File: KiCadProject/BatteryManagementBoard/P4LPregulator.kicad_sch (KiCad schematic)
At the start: 6 parts, among them U401 BD433M5FP

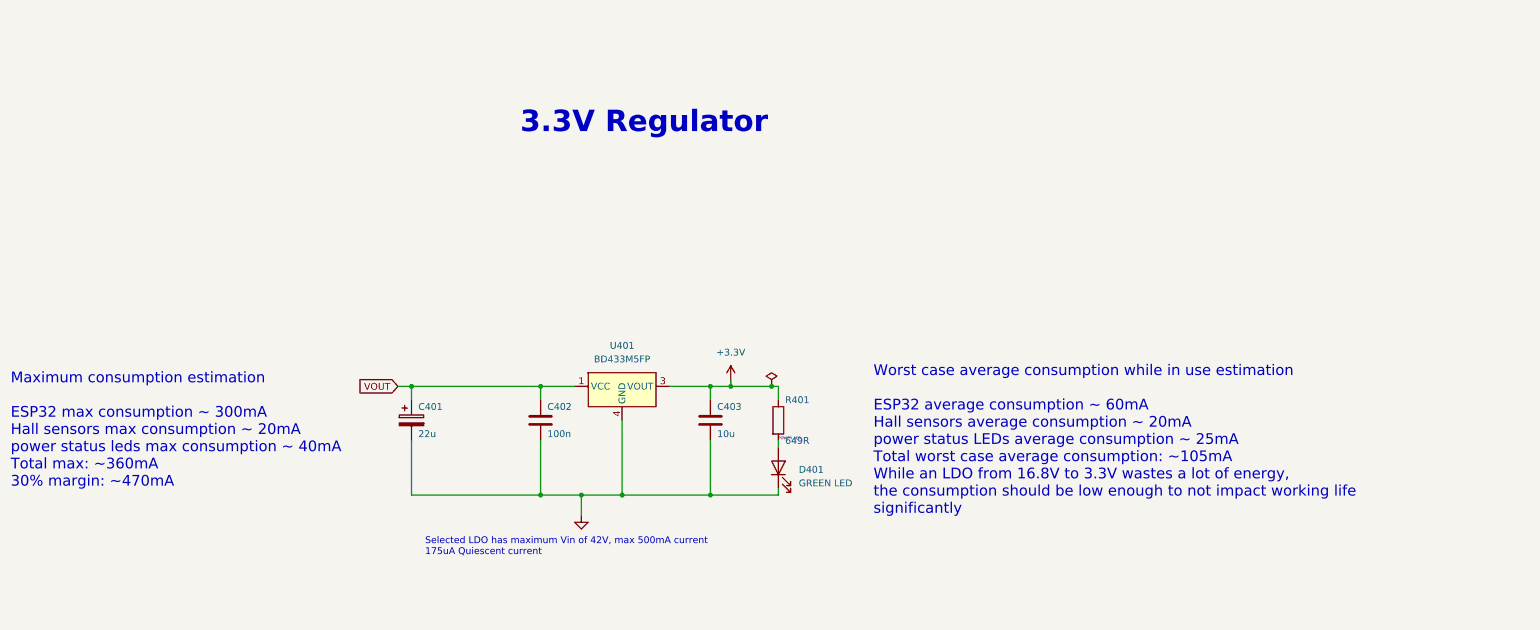
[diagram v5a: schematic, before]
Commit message: All PCB's should be done. Do a final check before ordering.
Signed-off-by: Eldalote.Electronics <Eldalote.Electronics@gmail.com>
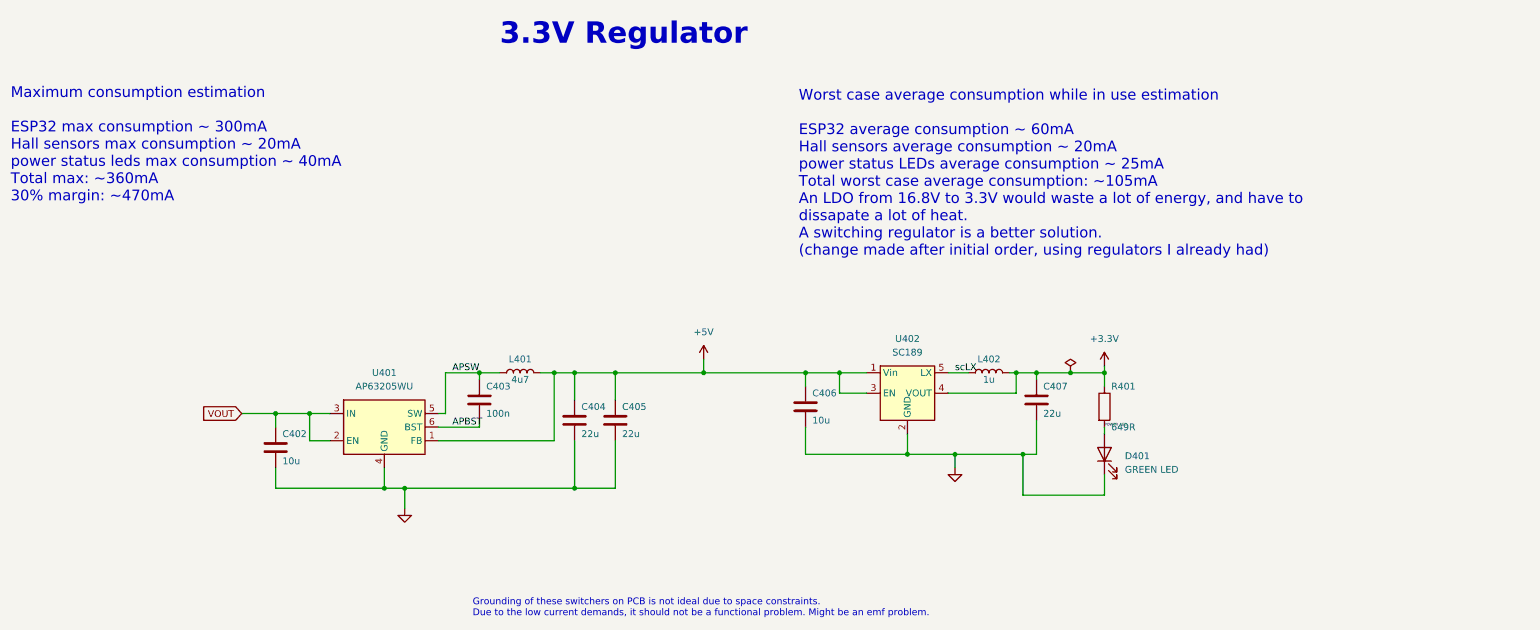
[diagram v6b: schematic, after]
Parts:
- removed C401: 22u, Capacitor_SMD:CP_Elec_5x5.3, symbol Device:C_Polarized
- removed U401: BD433M5FP, Package_TO_SOT_SMD:TO-252-3_TabPin4, symbol Eldalote_symbols:BD433M5FP
- added C404, C405, C407: 22u, Capacitor_SMD:C_0805_2012Metric, symbol Device:C
- added C406: 10u, Capacitor_SMD:C_0805_2012Metric, symbol Device:C
- added L401: 4u7, Inductor_SMD:L_1210_3225Metric, symbol Device:L
- added L402: 1u, Inductor_SMD:L_1210_3225Metric, symbol Device:L
- added U401: AP63205WU, Package_TO_SOT_SMD:TSOT-23-6, symbol Regulator_Switching:AP63205WU
- added U402: SC189, Package_TO_SOT_SMD:SOT-23-5, symbol Eldalote_symbols:SC189
- C402: value 100n -> 10u; footprint Capacitor_SMD:C_0402_1005Metric -> Capacitor_SMD:C_0805_2012Metric; Extra Requirement 25V -> (none); MfID CL05A104KA5NNNC -> (none)
- C403: value 10u -> 100n; footprint Capacitor_SMD:C_0805_2012Metric -> Capacitor_SMD:C_0402_1005Metric; Extra Requirement 25V -> (none); MfID CL21A106KAYNNNG -> (none)
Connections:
- net +3.3V: now also C407.1, L402.2, U402.4 (VOUT); no longer C403.1
- net GND: now also C404.2, C405.2, C406.2, C407.2, U401.4 (GND), U402.2 (GND); no longer C403.2
- net VOUT: now also U401.2 (EN), U401.3 (IN)
- new net +5V: C404.1, C405.1, C406.1, L401.2, U401.1 (FB), U402.1 (Vin), U402.3 (EN)
- new net APBST: C403.2, U401.6 (BST)
- new net APSW: C403.1, L401.1, U401.5 (SW)
- new net scLX: L402.1, U402.5 (LX)
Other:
- note added: "Grounding of these switchers on PCB is not ideal due to space constraints. Due to the low current demands, it should not be a functional problem. Might be an emf problem."
- note added: "Worst case average consumption while in use estimation ESP32 average consumption ~ 60mA Hall sensors average consumption ~ 20mA power status LEDs average consumption ~ 25mA Total worst case average consumption: ~105mA An LDO from 16.8V to 3.3V would waste a lot of energy, and have to dissapate a lot of heat. A switching regulator is a better solution. (change made after initial order, using regul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"
- note removed: "Selected LDO has maximum Vin of 42V, max 500mA current 175uA Quiescent current"
- note removed: "Worst case average consumption while in use estimation ESP32 average consumption ~ 60mA Hall sensors average consumption ~ 20mA power status LEDs average consumption ~ 25mA Total worst case average consumption: ~105mA While an LDO from 16.8V to 3.3V wastes a lot of energy, the consumption should be low enough to not impact working life significantly"
- moved on the sheet: D401, R401

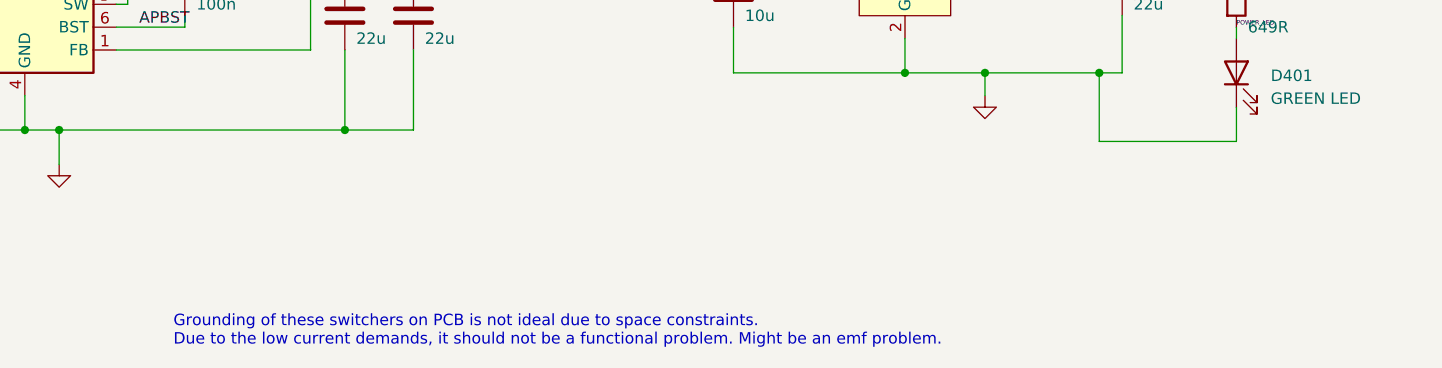
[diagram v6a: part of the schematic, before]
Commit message: Made ready to order PCBs. Some problems with ordering due to misunderstanding. Thinking about solutions
Signed-off-by: Eldalote.Electronics <Eldalote.Electronics@gmail.com>
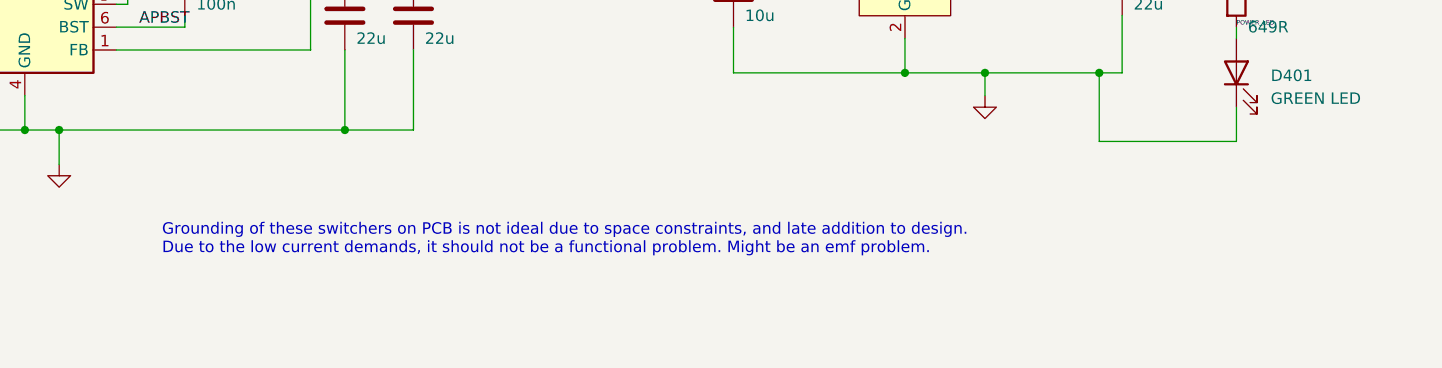
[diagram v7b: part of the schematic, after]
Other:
- note added: "Grounding of these switchers on PCB is not ideal due to space constraints, and late addition to design. Due to the low current demands, it should not be a functional problem. Might be an emf problem."
- note removed: "Grounding of these switchers on PCB is not ideal due to space constraints. Due to the low current demands, it should not be a functional problem. Might be an emf problem."
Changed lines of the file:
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@@
     (effects (font (size 2 2)) (justify left bottom))
   )
-  (text "Grounding of these switchers on PCB is not ideal due to space constraints.\nDue to the low current demands, it should not be a functional problem. Might be an emf problem."
-    (at 106.68 134.62 0)
+  (text "Grounding of these switchers on PCB is not ideal due to space constraints, and late addition to design.\nDue to the low current demands, it should not be a functional problem. Might be an emf problem."
+    (at 105.41 124.46 0)
     (effects (font (size 1.27 1.27)) (justify left bottom))
   )
